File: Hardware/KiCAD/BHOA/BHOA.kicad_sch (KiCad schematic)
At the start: 27 parts, among them J1 Bal Input, J10 Input SW L, J11 UnBal Input, J12 Input SW R, J2 Prestage SW R, J4 PWR, J5 Prestage SW L, J6 Output Stage Out, J8 SW Conn, J9 SW Conn

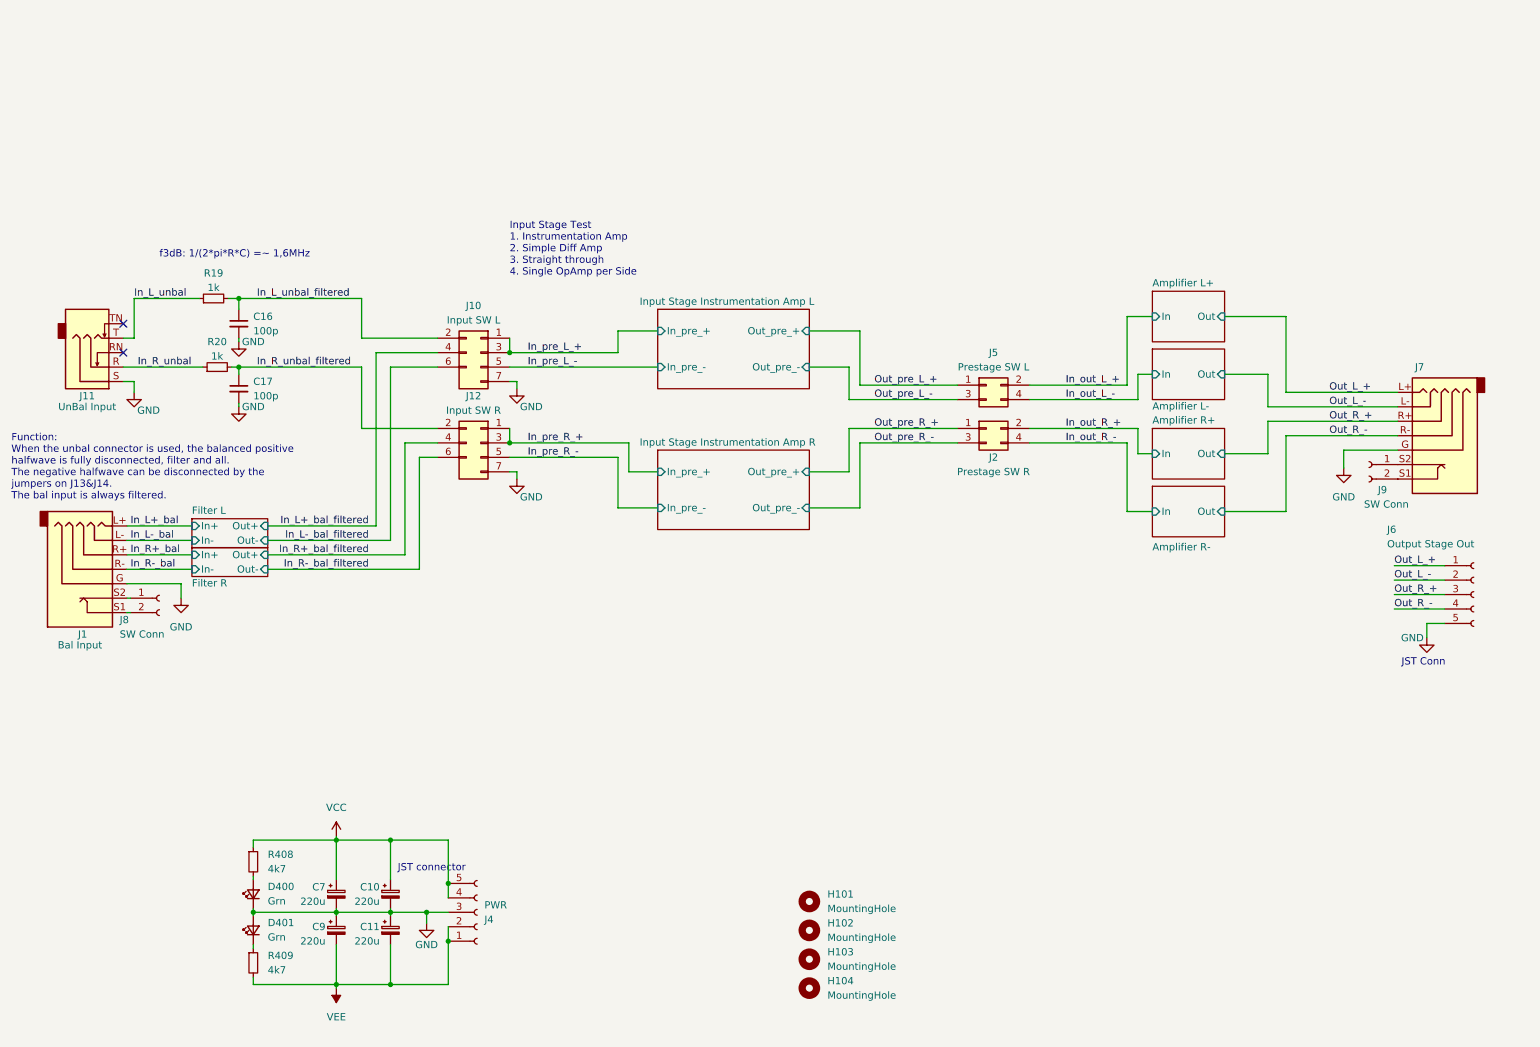
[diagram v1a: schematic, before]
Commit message: added outpout relays
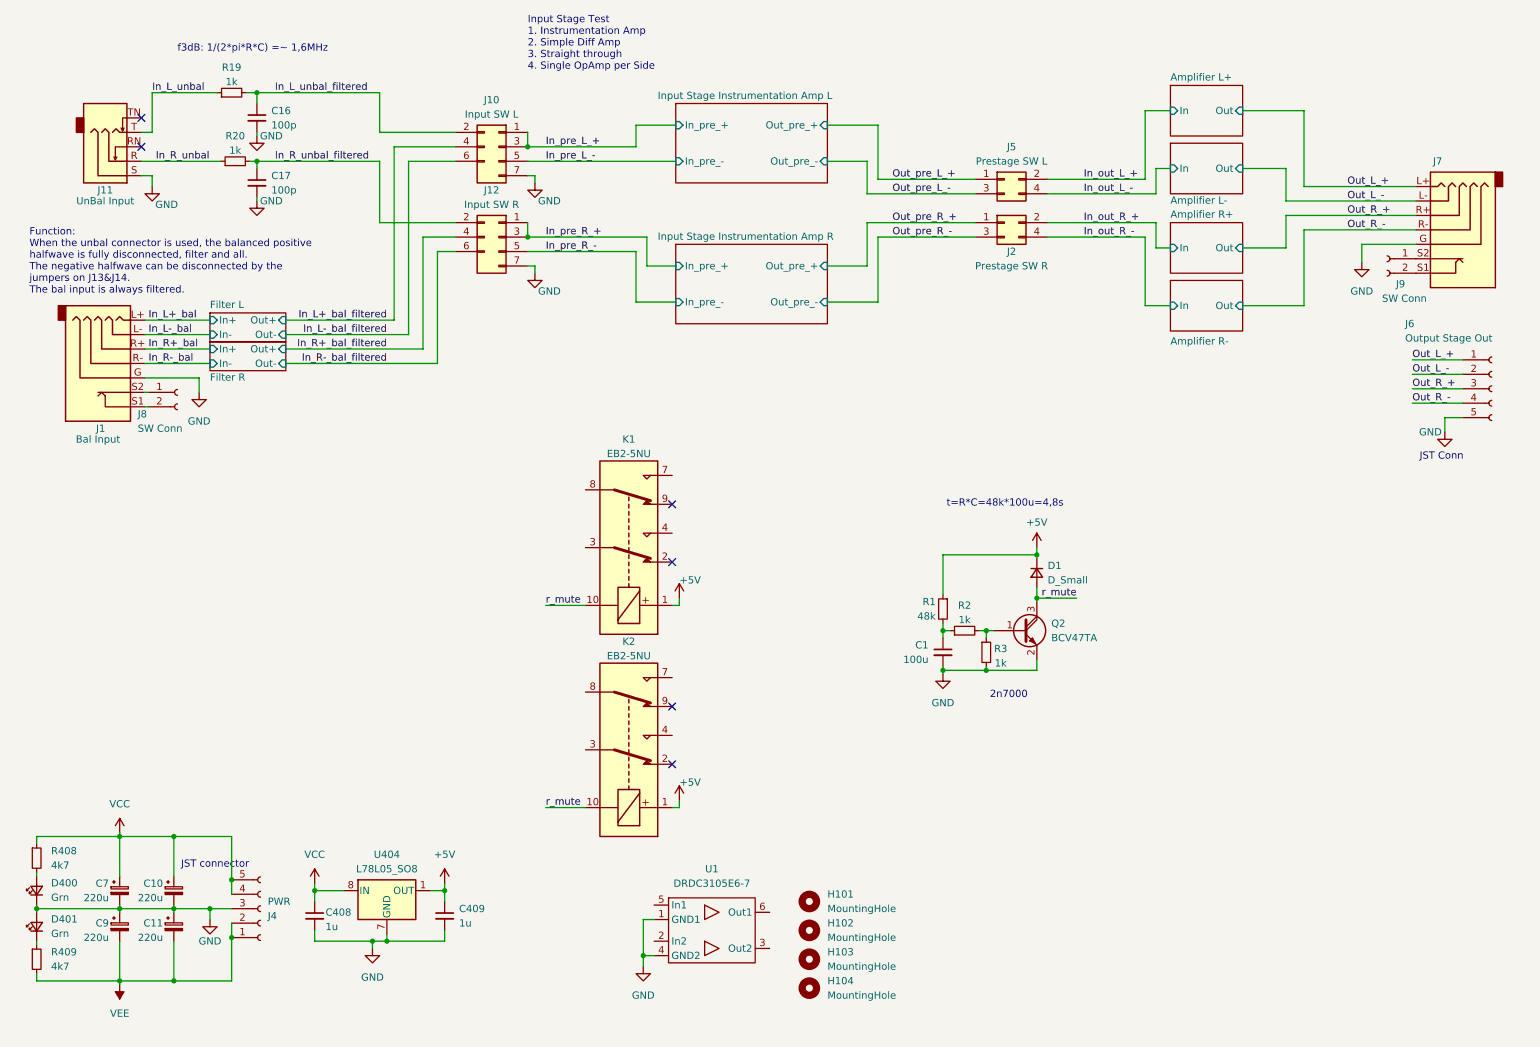
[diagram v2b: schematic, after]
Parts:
- added C1: 100u, Resistor_SMD:R_0805_2012Metric_Pad1.20x1.40mm_HandSolder, symbol Device:C_Small
- added C408, C409: 1u, Capacitor_SMD:C_0805_2012Metric_Pad1.18x1.45mm_HandSolder, symbol Device:C_Small
- added D1: D_Small, symbol Device:D_Small
- added K1, K2: EB2-5NU, Relay_SMD:Relay_DPDT_FRT5_SMD, symbol Relay:FRT5
- added Q2: BCV47TA, Package_TO_SOT_SMD:SOT-23, symbol Device:Q_NPN_Darlington_BEC
- added R1: 48k, symbol Device:R_Small
- added R2, R3: 1k, Resistor_SMD:R_0805_2012Metric_Pad1.20x1.40mm_HandSolder, symbol Device:R_Small
- added U1: DRDC3105E6-7, Package_TO_SOT_SMD:SOT-23-6_Handsoldering, symbol DRDC3105:DRDC3105E6-7
- added U404: L78L05_SO8, Package_SO:SOIC-8_3.9x4.9mm_P1.27mm, symbol Regulator_Linear:L78L05_SO8
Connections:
- net GND: now also C1.2, C408.2, C409.2, Q2.2 (E), R3.2, U1.1 (GND1), U1.4 (GND2), U404.2 (GND), U404.3 (GND), U404.6 (GND), U404.7 (GND)
- net VCC: now also C408.1, U404.8 (IN)
- new net: Q2.1 (B), R2.2, R3.1
- new net: C1.1, R1.2, R2.1
- new net +5V: C409.1, D1.1 (K), K1.1, K2.1, R1.1, U404.1 (OUT)
- new net r_mute: D1.2 (A), K1.10, K2.10, Q2.3 (C)
- no-connect marks 2 -> 6
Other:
- note added: "2n7000"
- note added: "t=R*C=48k*100u=4,8s"
- company: ncAudio -> C Audio
- title: NCBalOPHeadAmp -> BHOA
- moved on the sheet: C10, C11, C16, C17, C7, C9, D400, D401, J1, J10, J11, J12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

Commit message: Updated PCB with output protection
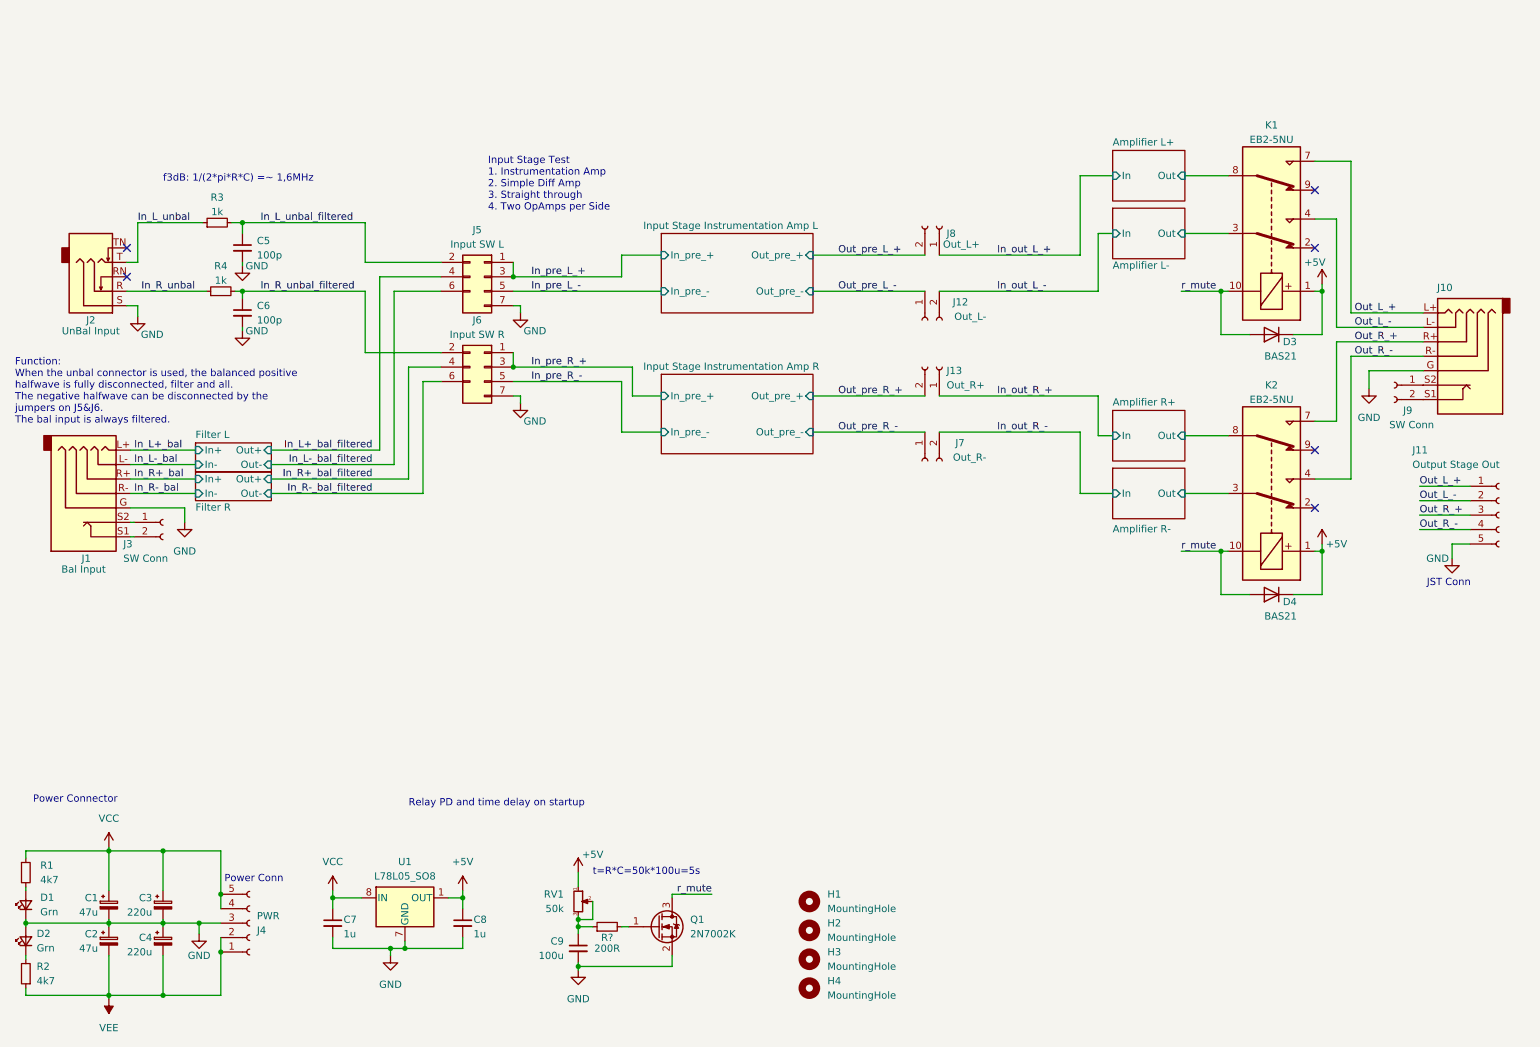
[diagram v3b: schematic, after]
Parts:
- removed C408, C409: 1u, Capacitor_SMD:C_0805_2012Metric_Pad1.18x1.45mm_HandSolder, symbol Device:C_Small
- removed C9: 220u, Capacitor_SMD:CP_Elec_8x10, symbol Device:C_Polarized_Small
- removed D1: D_Small, symbol Device:D_Small
- removed D400, D401: Grn, LED_SMD:LED_0805_2012Metric_Pad1.15x1.40mm_HandSolder, symbol Device:LED_Small
- removed J10: Input SW L, Connector_PinHeader_2.54mm:PinHeader_2x04_P2.54mm_Vertical, symbol Connector_Generic:Conn_2Rows-07Pins
- removed J12: Input SW R, Connector_PinHeader_2.54mm:PinHeader_2x04_P2.54mm_Vertical, symbol Connector_Generic:Conn_2Rows-07Pins
- removed J2: Prestage SW R, Connector_PinHeader_2.54mm:PinHeader_2x02_P2.54mm_Vertical, symbol Connector_Generic:Conn_02x02_Odd_Even
- removed J5: Prestage SW L, Connector_PinHeader_2.54mm:PinHeader_2x02_P2.54mm_Vertical, symbol Connector_Generic:Conn_02x02_Odd_Even
- removed Q2: BCV47TA, Package_TO_SOT_SMD:SOT-23, symbol Device:Q_NPN_Darlington_BEC
- removed R3: 1k, Resistor_SMD:R_0805_2012Metric_Pad1.20x1.40mm_HandSolder, symbol Device:R_Small
- removed R408, R409: 4k7, Resistor_SMD:R_0805_2012Metric_Pad1.20x1.40mm_HandSolder, symbol Device:R_Small
- removed U1: DRDC3105E6-7, Package_TO_SOT_SMD:SOT-23-6_Handsoldering, symbol DRDC3105:DRDC3105E6-7
- removed U404: L78L05_SO8, Package_SO:SOIC-8_3.9x4.9mm_P1.27mm, symbol Regulator_Linear:L78L05_SO8
- added C2: 47u, Capacitor_SMD:CP_Elec_6.3x5.8, symbol Device:C_Polarized_Small
- added C7, C8: 1u, Capacitor_SMD:C_0805_2012Metric_Pad1.18x1.45mm_HandSolder, symbol Device:C_Small
- added D1, D2: Grn, LED_SMD:LED_0805_2012Metric_Pad1.15x1.40mm_HandSolder, symbol Device:LED_Small
- added D3, D4: BAS21, Package_TO_SOT_SMD:SOT-23, symbol Diode:BAS21
- added J12: Out_L-, Connector_PinHeader_2.54mm:PinHeader_1x02_P2.54mm_Vertical, symbol Connector:Conn_01x02_Socket
- added J13: Out_R+, Connector_PinHeader_2.54mm:PinHeader_1x02_P2.54mm_Vertical, symbol Connector:Conn_01x02_Socket
- added J5: Input SW L, Connector_PinHeader_2.54mm:PinHeader_2x04_P2.54mm_Vertical, symbol Connector_Generic:Conn_2Rows-07Pins
- added J6: Input SW R, Connector_PinHeader_2.54mm:PinHeader_2x04_P2.54mm_Vertical, symbol Connector_Generic:Conn_2Rows-07Pins
- added J7: Out_R-, Connector_PinHeader_2.54mm:PinHeader_1x02_P2.54mm_Vertical, symbol Connector:Conn_01x02_Socket
- added J8: Out_L+, Connector_PinHeader_2.54mm:PinHeader_1x02_P2.54mm_Vertical, symbol Connector:Conn_01x02_Socket
- added Q1: 2N7002K, Package_TO_SOT_SMD:SOT-23, symbol Transistor_FET:2N7002K
- added R?: 200R, Resistor_SMD:R_0805_2012Metric_Pad1.20x1.40mm_HandSolder, symbol Device:R_Small
- added RV1: 50k, Potentiometer_SMD:Potentiometer_Bourns_TC33X_Vertical, symbol Device:R_Potentiometer_Small
- added U1: L78L05_SO8, Package_SO:SOIC-8_3.9x4.9mm_P1.27mm, symbol Regulator_Linear:L78L05_SO8
- C1: renamed from C7; value 220u -> 47u; footprint Capacitor_SMD:CP_Elec_8x10 -> Capacitor_SMD:CP_Elec_6.3x5.8; Mouser (none) -> 140-VZL470M1VTR-0606
- R1: value 48k -> 4k7; footprint (none) -> Resistor_SMD:R_0805_2012Metric_Pad1.20x1.40mm_HandSolder
- R2: value 1k -> 4k7
- renumbered C10 to C3, C11 to C4, C16 to C5, C17 to C6, C1 to C9, H101 to H1, H102 to H2, H103 to H3, H104 to H4, J7 to J10, J6 to J11, J11 to J2, J8 to J3, R19 to R3, R20 to R4
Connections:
- net +5V: now also C8.1, D3.3 (K), D4.3 (K), RV1.1, U1.1 (OUT); no longer R1.1
- net GND: now also C2.1, C7.2, C8.2, D1.1 (K), D2.2 (A), J5.7 (Pin_7), J6.7 (Pin_7), Q1.2 (S), U1.2 (GND), U1.3 (GND), U1.6 (GND), U1.7 (GND)
- net In_L+_bal_filtered: now also J5.4 (Pin_4)
- net In_L-_bal_filtered: now also J5.6 (Pin_6)
- net In_L_unbal_filtered: now also J5.2 (Pin_2)
- net In_R+_bal_filtered: now also J6.4 (Pin_4)
- net In_R-_bal_filtered: now also J6.6 (Pin_6)
- net In_R_unbal_filtered: now also J6.2 (Pin_2)
- net In_out_L_+: now also J8.1 (Pin_1)
- net In_out_L_-: now also J12.2 (Pin_2)
- net In_out_R_+: now also J13.1 (Pin_1)
- net In_out_R_-: now also J7.2 (Pin_2)
- net In_pre_L_+: now also J5.1 (Pin_1), J5.3 (Pin_3)
- net In_pre_L_-: now also J5.5 (Pin_5)
- net In_pre_R_+: now also J6.1 (Pin_1), J6.3 (Pin_3)
- net In_pre_R_-: now also J6.5 (Pin_5)
- net Out_L_+: now also K1.7
- net Out_L_-: now also K1.4
- net Out_R_+: now also K2.7
- net Out_R_-: now also K2.4
- net Out_pre_L_+: now also J8.2 (Pin_2)
- net Out_pre_L_-: now also J12.1 (Pin_1)
- net Out_pre_R_+: now also J13.2 (Pin_2)
- net Out_pre_R_-: now also J7.1 (Pin_1)
- net VCC: now also R1.1, C7.1, U1.8 (IN)
- net VEE: now also R2.1, C2.2
- net r_mute: now also D3.1 (A), D4.1 (A), Q1.3 (D)
- net at R2.2: now also D2.1 (K)
- net Amplifier L-/Out: now reaches K1.3
- net Amplifier L+/Out: now reaches K1.8
- net Amplifier R-/Out: now reaches K2.3
- net Amplifier R+/Out: now reaches K2.8
- new net: C9.1, R?.1, RV1.2, RV1.3
- new net: Q1.1 (G), R?.2
- new net: D1.2 (A), R1.2
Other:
- note added: "Function: When the unbal connector is used, the balanced positive halfwave is fully disconnected, filter and all. The negative halfwave can be disconnected by the jumpers on J5&J6. The bal input is always filtered."
- note added: "Input Stage Test 1. Instrumentation Amp 2. Simple Diff Amp 3. Straight through 4. Two OpAmps per Side"
- note added: "Power Conn"
- note added: "Power Connector"
- note added: "Relay PD and time delay on startup"
- note added: "t=R*C=50k*100u=5s"
- note removed: "2n7000"
- note removed: "Function: When the unbal connector is used, the balanced positive halfwave is fully disconnected, filter and all. The negative halfwave can be disconnected by the jumpers on J13&J14. The bal input is always filtered."
- note removed: "Input Stage Test 1. Instrumentation Amp 2. Simple Diff Amp 3. Straight through 4. Single OpAmp per Side"
- note removed: "JST connector"
- note removed: "t=R*C=48k*100u=4,8s"
- moved on the sheet: C1, C3, C4, C5, C6, C9, J1, J10, J11, J2, J3, J4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

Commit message: housekeeping
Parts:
- added H5: MountingHole, MountingHole:MountingHole_3.7mm, symbol Mechanical:MountingHole
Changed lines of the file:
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@@
+    )
+  )
+  (symbol (lib_id "Mechanical:MountingHole") (at 154.94 193.675 0) (unit 1)
+    (in_bom yes) (on_board yes) (dnp no) (fields_autoplaced)
+    (property "Reference" "H5" (at 158.115 192.405 0)
+      (effects (font (size 1.27 1.27)) (justify left))
+    )
+    (property "Value" "MountingHole" (at 158.115 194.945 0)
+      (effects (font (size 1.27 1.27)) (justify left))
+    )
+    (property "Footprint" "MountingHole:MountingHole_3.7mm" (at 154.94 193.675 0)
+      (effects (font (size 1.27 1.27)) hide)
+    )
+    (property "Datasheet" "~" (at 154.94 193.675 0)
+      (effects (font (size 1.27 1.27)) hide)
+    )
+    (instances
+      (project "BHOA"
+        (path "/c3692abe-17e6-4ebd-8bee-103b4ec28f89"
+          (reference "H5") (unit 1)
+        )
+      )
     )
   )
